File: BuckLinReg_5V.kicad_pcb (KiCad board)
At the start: 4 copper layers, 96 x 56 mm, 70 parts, among them J1 Barrel_Jack, J2 796638-4, J3 1x2 Male, Q1 PMBT2222, Q2 SQD40061EL, SW1 SW_SPDT, U1 TLV76050DBZT, U2 LMV358, U3 74HCT00, U4 SN74HCT02, U5 TCM810, U6 TPS56339DDC, U7 LM1084-5.0

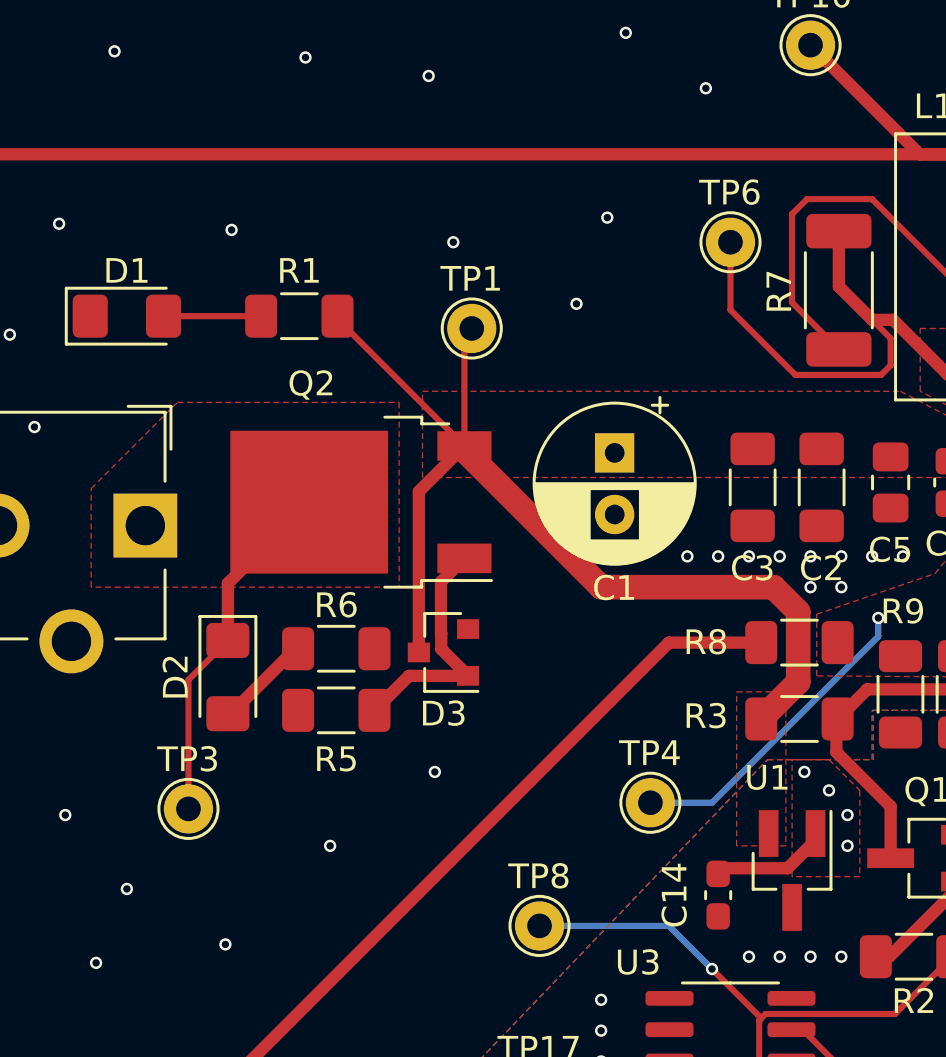
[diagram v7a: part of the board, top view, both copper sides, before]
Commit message: Moved some test points to allow for better ground high current return path
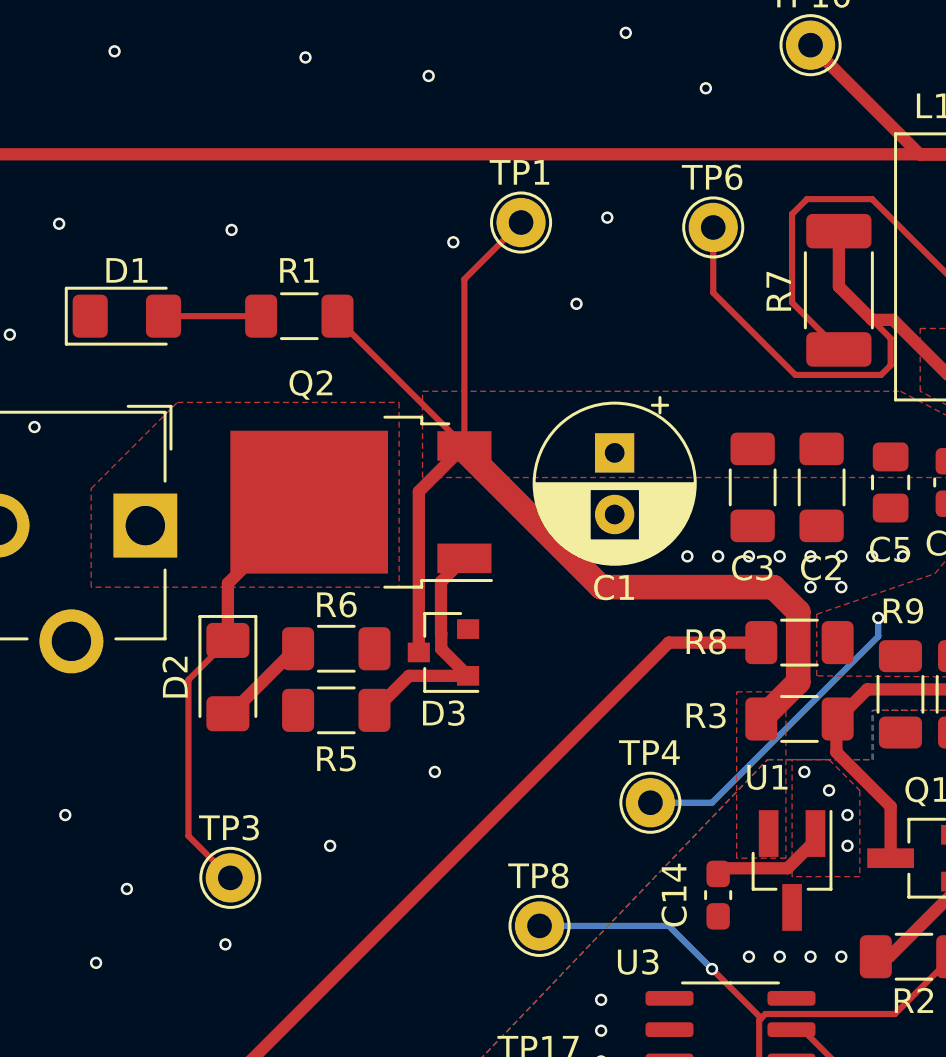
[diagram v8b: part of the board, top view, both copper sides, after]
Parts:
- moved TP1 4.74 mm to (88.0, 62.2)
- moved TP3 3.28 mm to (76.2, 88.8)
- moved TP6 0.92 mm to (95.8, 62.4)
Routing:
- net /+Vin: track 42.9 -> 48.0 mm
- net /Vin: track 14.5 -> 18.0 mm
- net /SW: track 23.9 -> 24.8 mm
